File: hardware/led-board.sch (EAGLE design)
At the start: 22 parts, among them U1 ATTINY84-20SSU

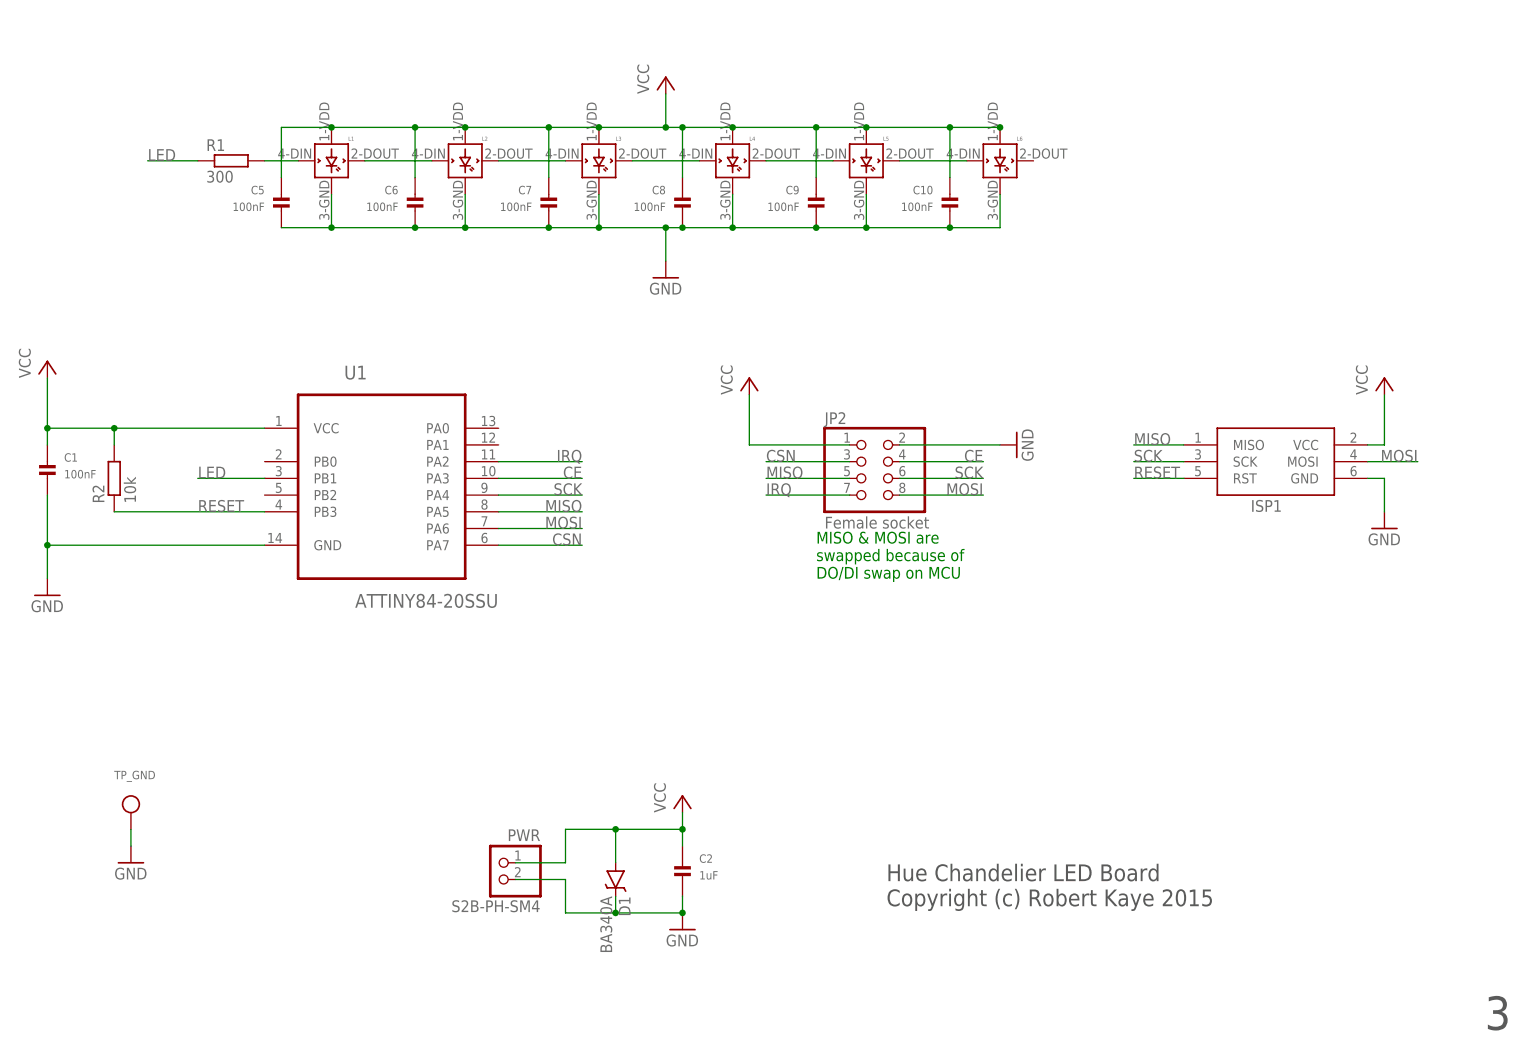
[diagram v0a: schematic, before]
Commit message: Last version of the arduino code with nurfl stuff. New layout without nurfl.
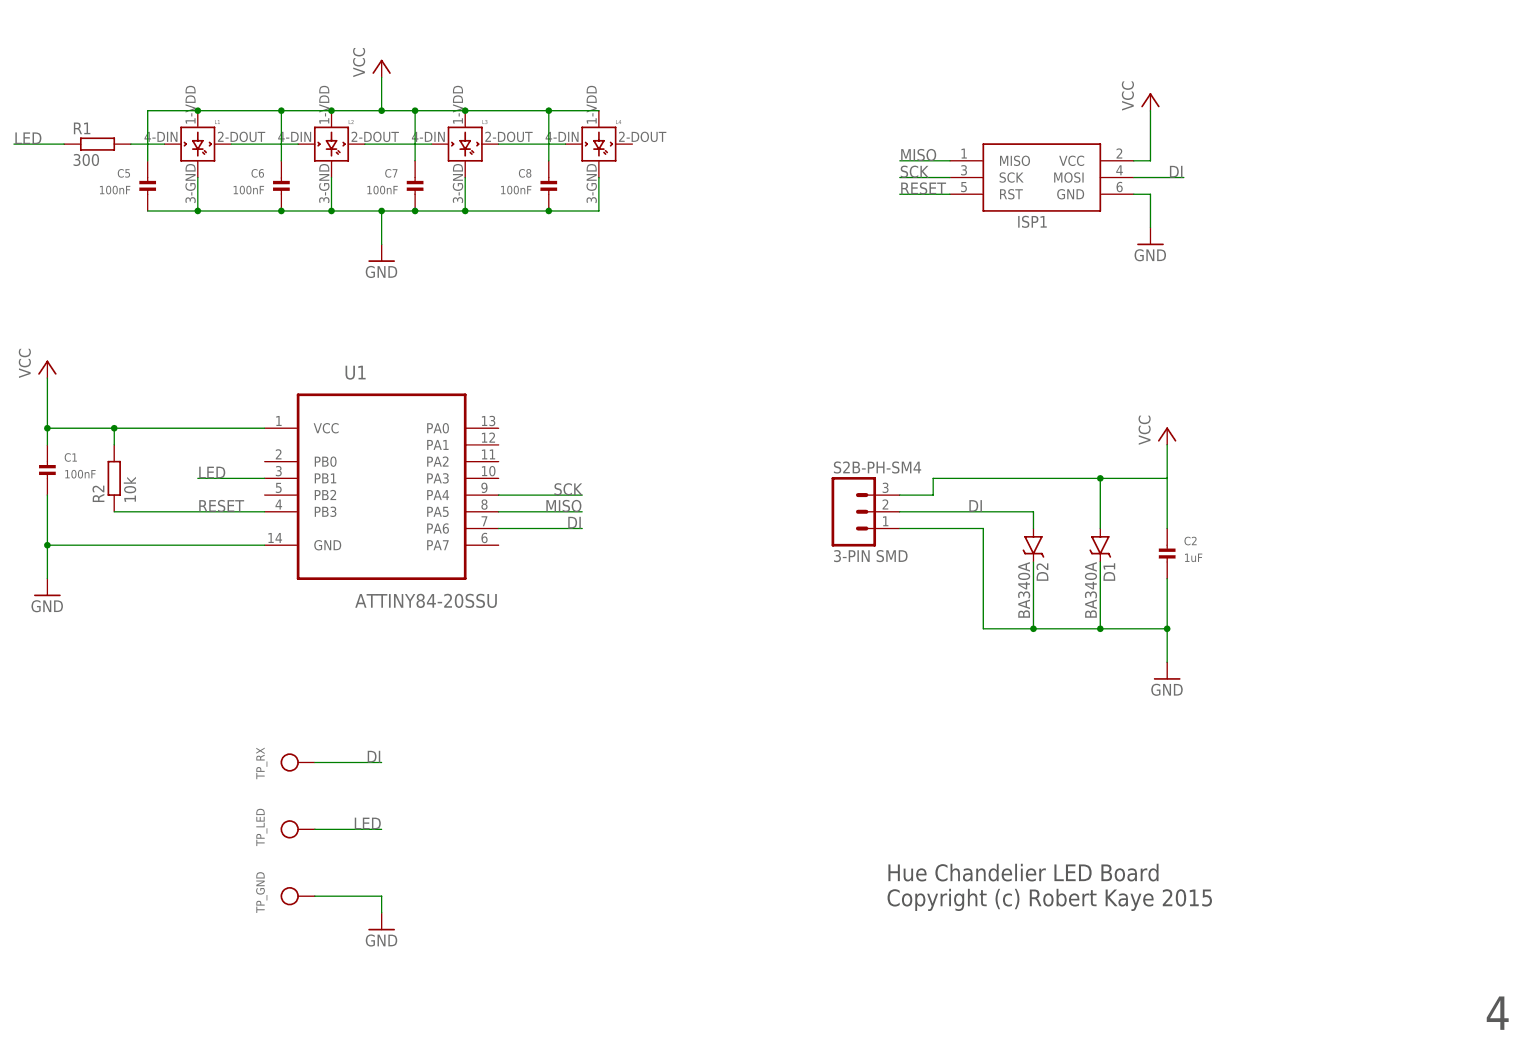
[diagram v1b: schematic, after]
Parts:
- removed C10, C9: 100nF, microbuilder:CAP_CERAMIC0805
- removed JP2: Female socket, adafruit:PINHD-2X4
- removed L5, L6: WS2812B, adafruit:WS2812B
- added D2: BA340A, SparkFun-DiscreteSemi:B340A
- added TP_LED, TP_RX: (no value), microbuilder:TESTPOINT1.5X2.0MM_NOCREAM
- S2B-PH-SM4: value PWR -> 3-PIN SMD; device adafruit:JST_2PIN-SMT-RA -> SparkFun-Connectors:M03JST-SMD
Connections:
- removed net CE: JP2.4, U1.PA3
- removed net CSN: JP2.3, U1.PA7
- removed net IRQ: JP2.7, U1.PA2
- removed net MOSI: ISP1.MOSI, JP2.8, U1.PA6
- removed net N$3: L5.DOUT, L6.DIN
- removed net N$7: L4.DOUT, L5.DIN
- new net DI: D2.A, ISP1.MOSI, S2B-PH-SM4.2, TP_RX.P$1, U1.PA6
- net GND: now also D2.C; no longer C10.P$2, C9.P$2, JP2.2, L5.GND, L6.GND
- net LED: now also TP_LED.P$1
- net MISO: no longer JP2.5
- net SCK: no longer JP2.6
- net VCC: now also S2B-PH-SM4.3; no longer C10.P$1, C9.P$1, JP2.1, L5.VDD, L6.VDD, S2B-PH-SM4.2
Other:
- note added: "4"
- note removed: "3"
- note removed: "MISO & MOSI are swapped because of DO/DI swap on MCU"
- moved on the sheet: C2, C5, C6, C7, C8, D1, ISP1, L1, L2, L3, L4, R1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

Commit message: Basic working node code, updated schematic and layout
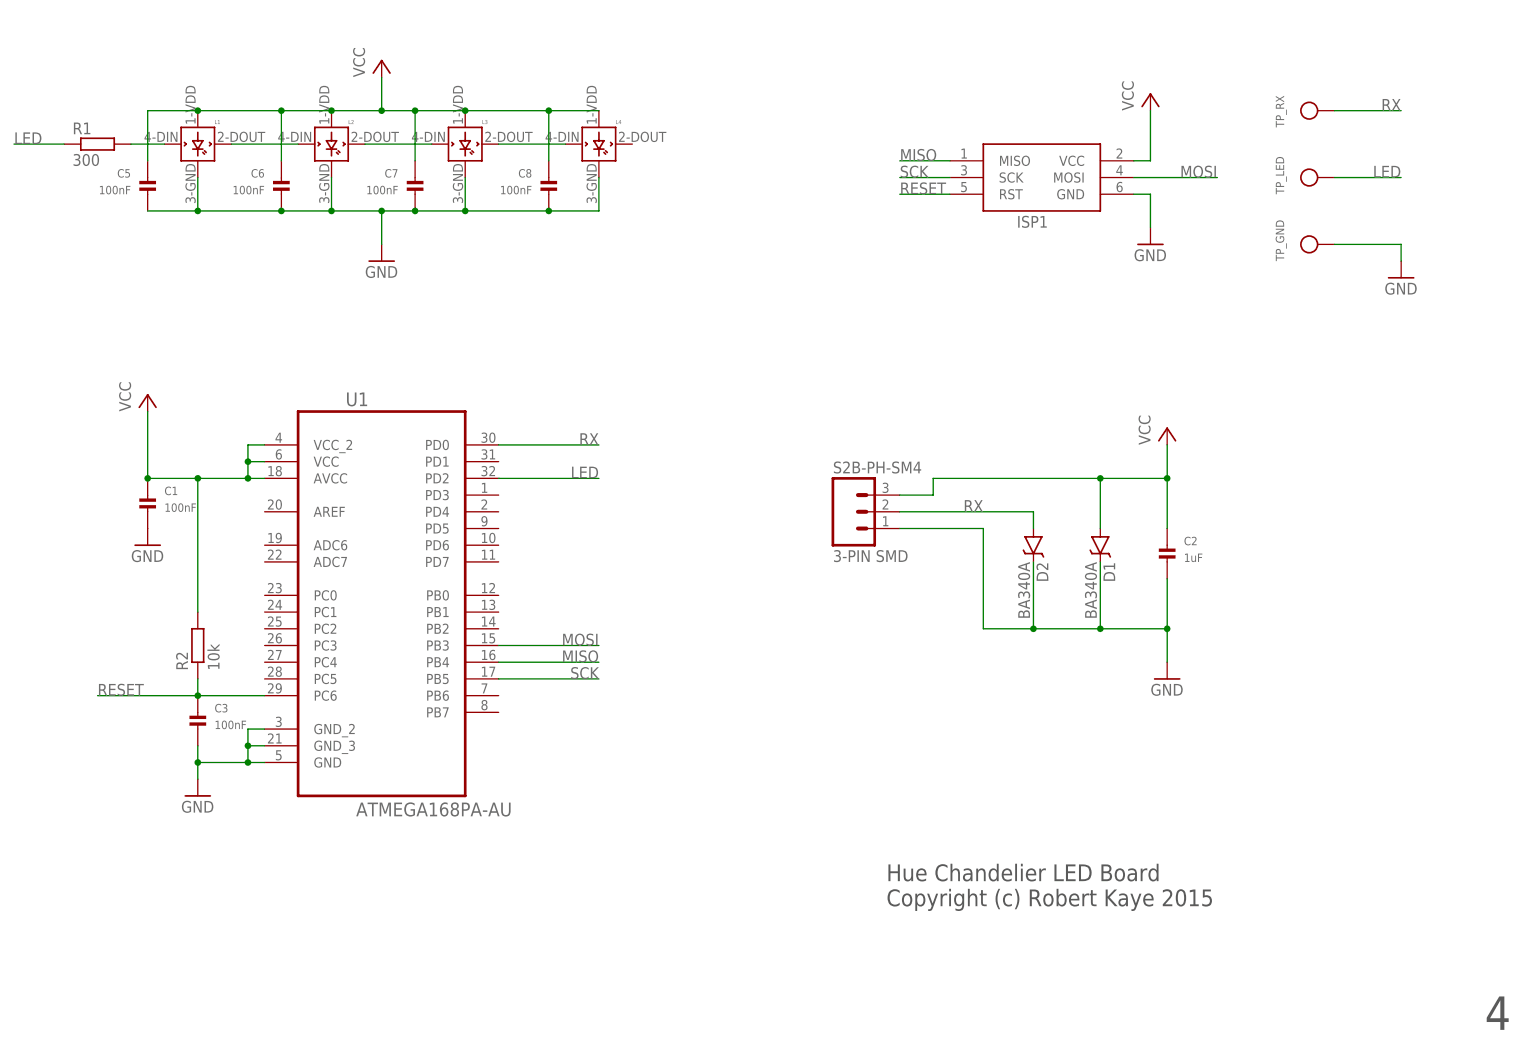
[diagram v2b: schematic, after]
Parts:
- added C3: 100nF, microbuilder:CAP_CERAMIC0805
- U1: value ATTINY84-20SSU -> ATMEGA168PA-AU; device Atmel_By_element14_Batch_1-00:ATTINY84-20SSU -> Atmel_By_element14_Batch_1-00:ATMEGA168PA-AU
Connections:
- removed net DI: D2.A, ISP1.MOSI, S2B-PH-SM4.2, TP_RX.P$1, U1.PA6
- new net MOSI: ISP1.MOSI, U1.PB3
- new net RX: D2.A, S2B-PH-SM4.2, TP_RX.P$1, U1.PD0
- net GND: now also C3.P$2, U1.GND_2, U1.GND_3
- net LED: now also U1.PD2; no longer U1.PB1
- net MISO: now also U1.PB4; no longer U1.PA5
- net RESET: now also C3.P$1, U1.PC6; no longer U1.PB3
- net SCK: now also U1.PB5; no longer U1.PA4
- net VCC: now also U1.AVCC, U1.VCC_2
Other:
- moved on the sheet: C1, R2, TP_GND, TP_LED, TP_RX

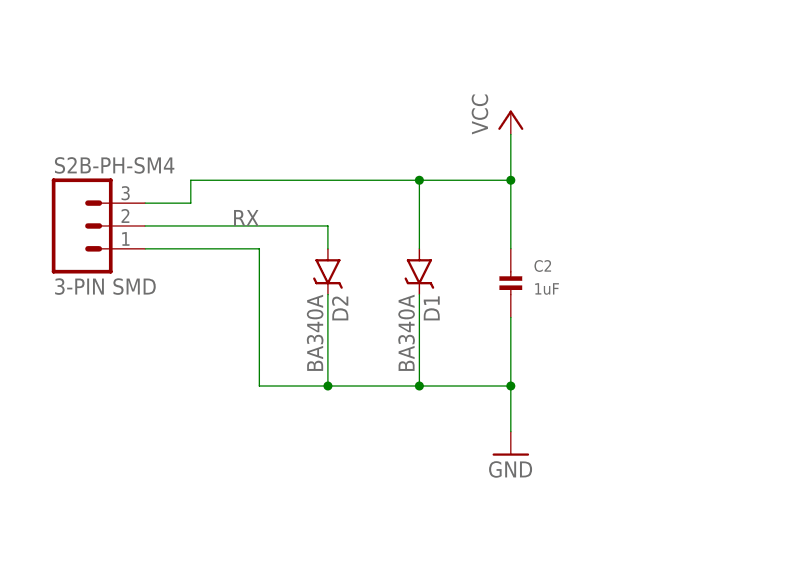
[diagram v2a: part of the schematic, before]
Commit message: Fixed the orientation of the shottky diodes, improved the layout a bit
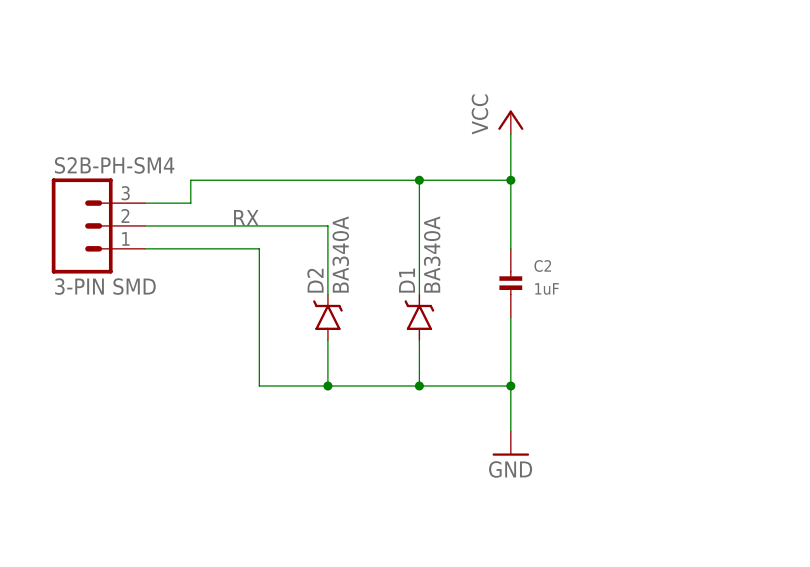
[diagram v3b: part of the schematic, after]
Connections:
- net GND: now also D1.A, D2.A; no longer D1.C, D2.C
- net RX: now also D2.C; no longer D2.A
- net VCC: now also D1.C; no longer D1.A
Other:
- moved on the sheet: D1, D2
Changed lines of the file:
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@@
 <instance part="FRAME1" gate="G$2" x="63.5" y="-48.26"/>
 <instance part="C2" gate="G$1" x="109.22" y="30.48"/>
-<instance part="D1" gate="G$1" x="99.06" y="33.02" rot="R270"/>
+<instance part="D1" gate="G$1" x="99.06" y="27.94" rot="R90"/>
 <instance part="TP_GND" gate="G$1" x="134.62" y="78.74" rot="R90"/>
 <instance part="GND4" gate="1" x="144.78" y="73.66"/>
 <instance part="TP_LED" gate="G$1" x="134.62" y="88.9" rot="R90"/>
 <instance part="TP_RX" gate="G$1" x="134.62" y="99.06" rot="R90"/>
-<instance part="D2" gate="G$1" x="88.9" y="33.02" rot="R270"/>
+<instance part="D2" gate="G$1" x="88.9" y="27.94" rot="R90"/>
 <instance part="C3" gate="G$1" x="-38.1" y="5.08"/>
 <instance part="GND5" gate="1" x="-45.72" y="33.02"/>
@@
 <wire x1="81.28" y1="20.32" x2="88.9" y2="20.32" width="0.1524" layer="91"/>
 <wire x1="88.9" y1="20.32" x2="99.06" y2="20.32" width="0.1524" layer="91"/>
+<wire x1="99.06" y1="20.32" x2="109.22" y2="20.32" width="0.1524" layer="91"/>
 <wire x1="81.28" y1="35.56" x2="81.28" y2="20.32" width="0.1524" layer="91"/>
 <pinref part="S2B-PH-SM4" gate="G$1" pin="1"/>
 <wire x1="68.58" y1="35.56" x2="81.28" y2="35.56" width="0.1524" layer="91"/>
-<pinref part="D1" gate="G$1" pin="C"/>
-<wire x1="99.06" y1="30.48" x2="99.06" y2="20.32" width="0.1524" layer="91"/>
-<pinref part="D2" gate="G$1" pin="C"/>
-<wire x1="88.9" y1="30.48" x2="88.9" y2="20.32" width="0.1524" layer="91"/>
 <pinref part="C2" gate="G$1" pin="P$2"/>
 <wire x1="109.22" y1="27.94" x2="109.22" y2="20.32" width="0.1524" layer="91"/>
-<wire x1="109.22" y1="20.32" x2="99.06" y2="20.32" width="0.1524" layer="91"/>
-<junction x="88.9" y="20.32"/>
-<junction x="99.06" y="20.32"/>
 <pinref part="GND1" gate="1" pin="GND"/>
 <wire x1="109.22" y1="20.32" x2="109.22" y2="15.24" width="0.1524" layer="91"/>
 <junction x="109.22" y="20.32"/>
+<pinref part="D2" gate="G$1" pin="A"/>
+<wire x1="88.9" y1="25.4" x2="88.9" y2="20.32" width="0.1524" layer="91"/>
+<pinref part="D1" gate="G$1" pin="A"/>
+<wire x1="99.06" y1="25.4" x2="99.06" y2="20.32" width="0.1524" layer="91"/>
+<junction x="99.06" y="20.32"/>
+<junction x="88.9" y="20.32"/>
 </segment>
 <segment>
@@
 </segment>
 <segment>
-<wire x1="99.06" y1="43.18" x2="109.22" y2="43.18" width="0.1524" layer="91"/>
 <wire x1="109.22" y1="35.56" x2="109.22" y2="43.18" width="0.1524" layer="91"/>
 <pinref part="C2" gate="G$1" pin="P$1"/>
-<pinref part="D1" gate="G$1" pin="A"/>
-<wire x1="99.06" y1="35.56" x2="99.06" y2="43.18" width="0.1524" layer="91"/>
-<junction x="99.06" y="43.18"/>
 <pinref part="S2B-PH-SM4" gate="G$1" pin="3"/>
 <wire x1="68.58" y1="40.64" x2="73.66" y2="40.64" width="0.1524" layer="91"/>
@@
 <wire x1="73.66" y1="43.18" x2="99.06" y2="43.18" width="0.1524" layer="91"/>
 <pinref part="P+2" gate="VCC" pin="VCC"/>
+<wire x1="99.06" y1="43.18" x2="109.22" y2="43.18" width="0.1524" layer="91"/>
 <wire x1="109.22" y1="43.18" x2="109.22" y2="48.26" width="0.1524" layer="91"/>
 <junction x="109.22" y="43.18"/>
+<pinref part="D1" gate="G$1" pin="C"/>
+<wire x1="99.06" y1="30.48" x2="99.06" y2="43.18" width="0.1524" layer="91"/>
+<junction x="99.06" y="43.18"/>
 </segment>
 <segment>
@@
 <wire x1="68.58" y1="38.1" x2="88.9" y2="38.1" width="0.1524" layer="91"/>
 <label x="81.28" y="38.1" size="1.778" layer="95" rot="MR0"/>
-<pinref part="D2" gate="G$1" pin="A"/>
-<wire x1="88.9" y1="38.1" x2="88.9" y2="35.56" width="0.1524" layer="91"/>
-</segment>
-</net>
+<pinref part="D2" gate="G$1" pin="C"/>
+<wire x1="88.9" y1="38.1" x2="88.9" y2="30.48" width="0.1524" layer="91"/>
+</segment>
+</net>

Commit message: Finished layot and silkscreening. Hopefully ready to go!
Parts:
- added TP_RX1: (no value), microbuilder:TESTPOINT1.5X2.0MM_NOCREAM
- C1, C3, C5, C6, C7, C8: MPN (none) -> MCSH21B104K250CT; OC_NEWARK (none) -> 23T7445
- C2: MPN (none) -> CC0805KKX7R7BB105; OC_NEWARK (none) -> 68R4880
- D1, D2: MPN (none) -> B330A-13-F; OC_NEWARK (none) -> 12T1463
- ISP, TP_GND, TP_LED, TP_RX: OC_NEWARK (none) -> unknown
- L1, L2, L3, L4: MPN (none) -> WS2812B; OC_NEWARK (none) -> 43Y4720
- R1: MF (none) -> Multicomp Passives; MPN (none) -> MC01W08051300R; OC_NEWARK (none) -> 58K4799
- R2: MPN (none) -> RT0805FRE0710KL; OC_NEWARK (none) -> 62M2341
- S2B-PH-SM4: MF (none) -> FARNELL; MPN (none) -> S3B-PH-SM4-TB(LF)(SN); OC_NEWARK (none) -> 38K8071
- U1: OC_NEWARK (none) -> 68T2717
- renumbered ISP1 to ISP
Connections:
- net VCC: now also TP_RX1.P$1

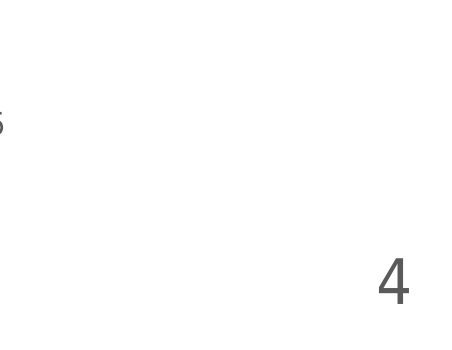
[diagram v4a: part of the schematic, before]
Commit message: Updated based on Bernard's feedback: Moved parts from the back to the front and moved one via out from under the mcu. Also ensured that no parts are close to the edges.
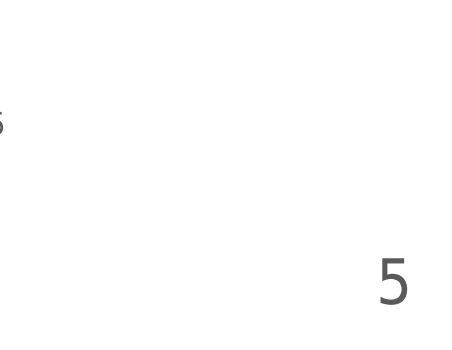
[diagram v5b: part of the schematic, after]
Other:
- note added: "5"
- note removed: "4"
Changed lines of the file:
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@@
 <sheet>
 <plain>
-<text x="157.48" y="-40.64" size="5.08" layer="97">4</text>
+<text x="157.48" y="-40.64" size="5.08" layer="97">5</text>
 <text x="66.548" y="-21.844" size="2.54" layer="97">Hue Chandelier LED Board
 Copyright (c) Robert Kaye 2015</text>

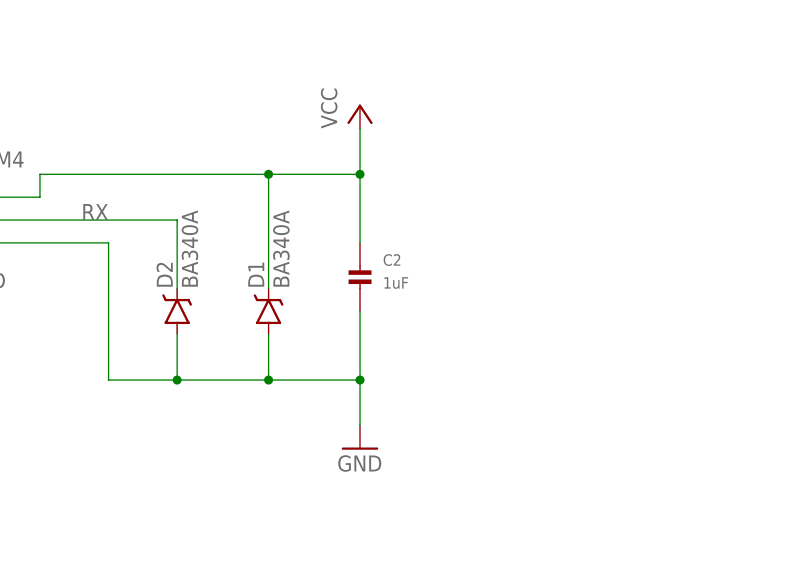
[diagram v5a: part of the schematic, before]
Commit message: Increased bulk capacitance (C1) to 47uF.
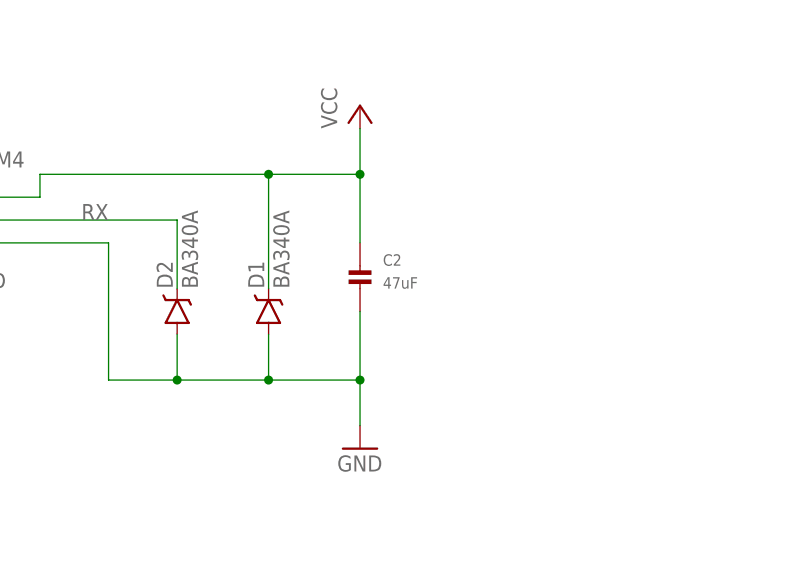
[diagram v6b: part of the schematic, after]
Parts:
- C2: value 1uF -> 47uF; device microbuilder:CAP_CERAMIC0805 -> microbuilder:CAP_CERAMIC1206
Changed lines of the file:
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@@
 </part>
 <part name="FRAME1" library="frames" deviceset="DINA4_L" device=""/>
-<part name="C2" library="microbuilder" deviceset="CAP_CERAMIC" device="0805" value="1uF">
+<part name="C2" library="microbuilder" deviceset="CAP_CERAMIC" device="1206" value="47uF">
 <attribute name="MF" value=""/>
 <attribute name="MPN" value="CC0805KKX7R7BB105"/>
